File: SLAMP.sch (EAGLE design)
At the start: 45 parts, among them IC1 MEGA8-AI, J1 CARA1, J2 CARA4, J3 CARA2, J4 CARA5, J5 CARA3, J6 EXTRA-D12, J7 A0, Q1 2N7002PW, U1 HC_05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

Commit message: Placa empezada
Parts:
- JP2: value (none) -> CTS/RTS-bt
- JP3: value (none) -> POWER
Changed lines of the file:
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@@
 <part name="SUPPLY5" library="SparkFun-Aesthetics" deviceset="3.3V" device=""/>
 <part name="GND8" library="SparkFun-Aesthetics" deviceset="GND" device=""/>
-<part name="JP2" library="pinhead" deviceset="PINHD-1X2" device=""/>
+<part name="JP2" library="pinhead" deviceset="PINHD-1X2" device="" value="CTS/RTS-bt"/>
 <part name="GND9" library="SparkFun-Aesthetics" deviceset="GND" device=""/>
 <part name="SUPPLY1" library="SparkFun-Aesthetics" deviceset="5V" device=""/>
@@
 <part name="R5" library="SparkFun-Passives" deviceset="RESISTOR" device="0805-RES" value="1k"/>
 <part name="SUPPLY4" library="SparkFun-Aesthetics" deviceset="3.3V" device=""/>
-<part name="JP3" library="pinhead" deviceset="PINHD-1X2" device=""/>
+<part name="JP3" library="pinhead" deviceset="PINHD-1X2" device="" value="POWER"/>
 <part name="GND10" library="SparkFun-Aesthetics" deviceset="GND" device=""/>
 <part name="SUPPLY6" library="SparkFun-Aesthetics" deviceset="5V" device=""/>

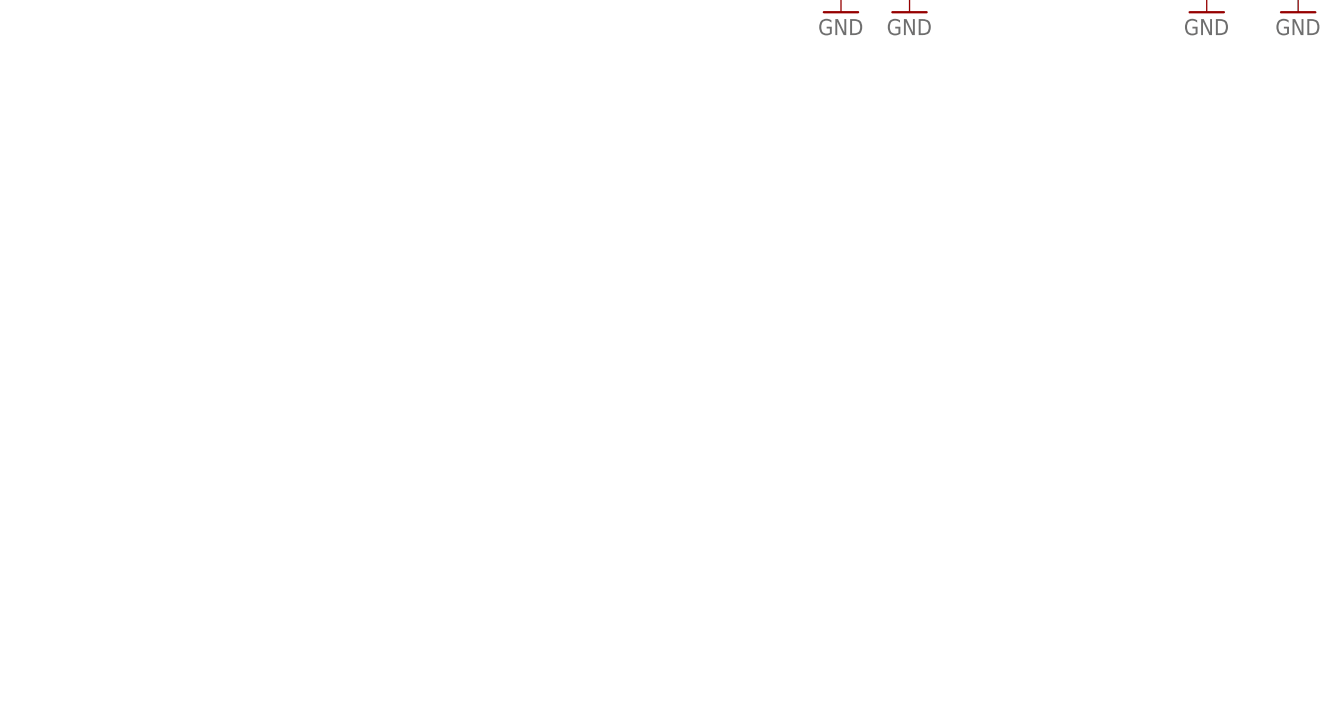
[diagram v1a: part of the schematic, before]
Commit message: capacitive touch sensor added
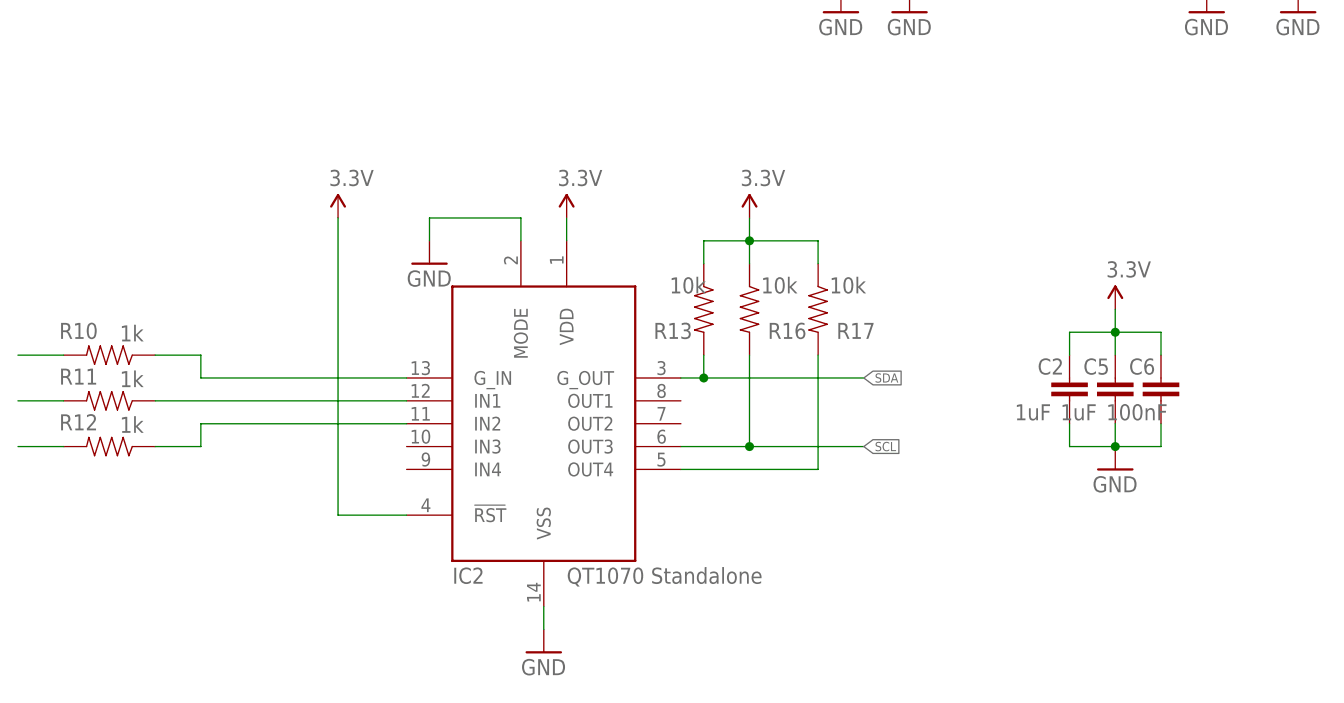
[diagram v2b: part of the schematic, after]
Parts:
- added C2, C5: 1uF, SparkFun-Passives:CAP0603-CAP
- added C6: 100nF, SparkFun-Passives:CAP0603-CAP
- added IC2: AT42QT1070-SSU, adafruit:AT42QT1070-SSU
- added R10, R11, R12: 1k, SparkFun-Passives:RESISTOR0603-RES
- added R13, R16, R17: 10k, SparkFun-Passives:RESISTOR0603-RES
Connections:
- new net N$1: IC2.OUT4, R17.2
- new net N$11: IC2.IN2, R12.1
- new net N$19: R10.2
- new net N$20: R11.2
- new net N$21: R12.2
- new net N$8: IC2.G_IN, R10.1
- new net N$9: IC2.IN1, R11.1
- new net SCL: IC2.OUT3, R16.2
- new net SDA: IC2.G_OUT, R13.2
- net 3.3V: now also C2.1, C5.1, C6.1, IC2.!RST, IC2.VDD, R13.1, R16.1, R17.1
- net GND: now also C2.2, C5.2, C6.2, IC2.MODE, IC2.VSS

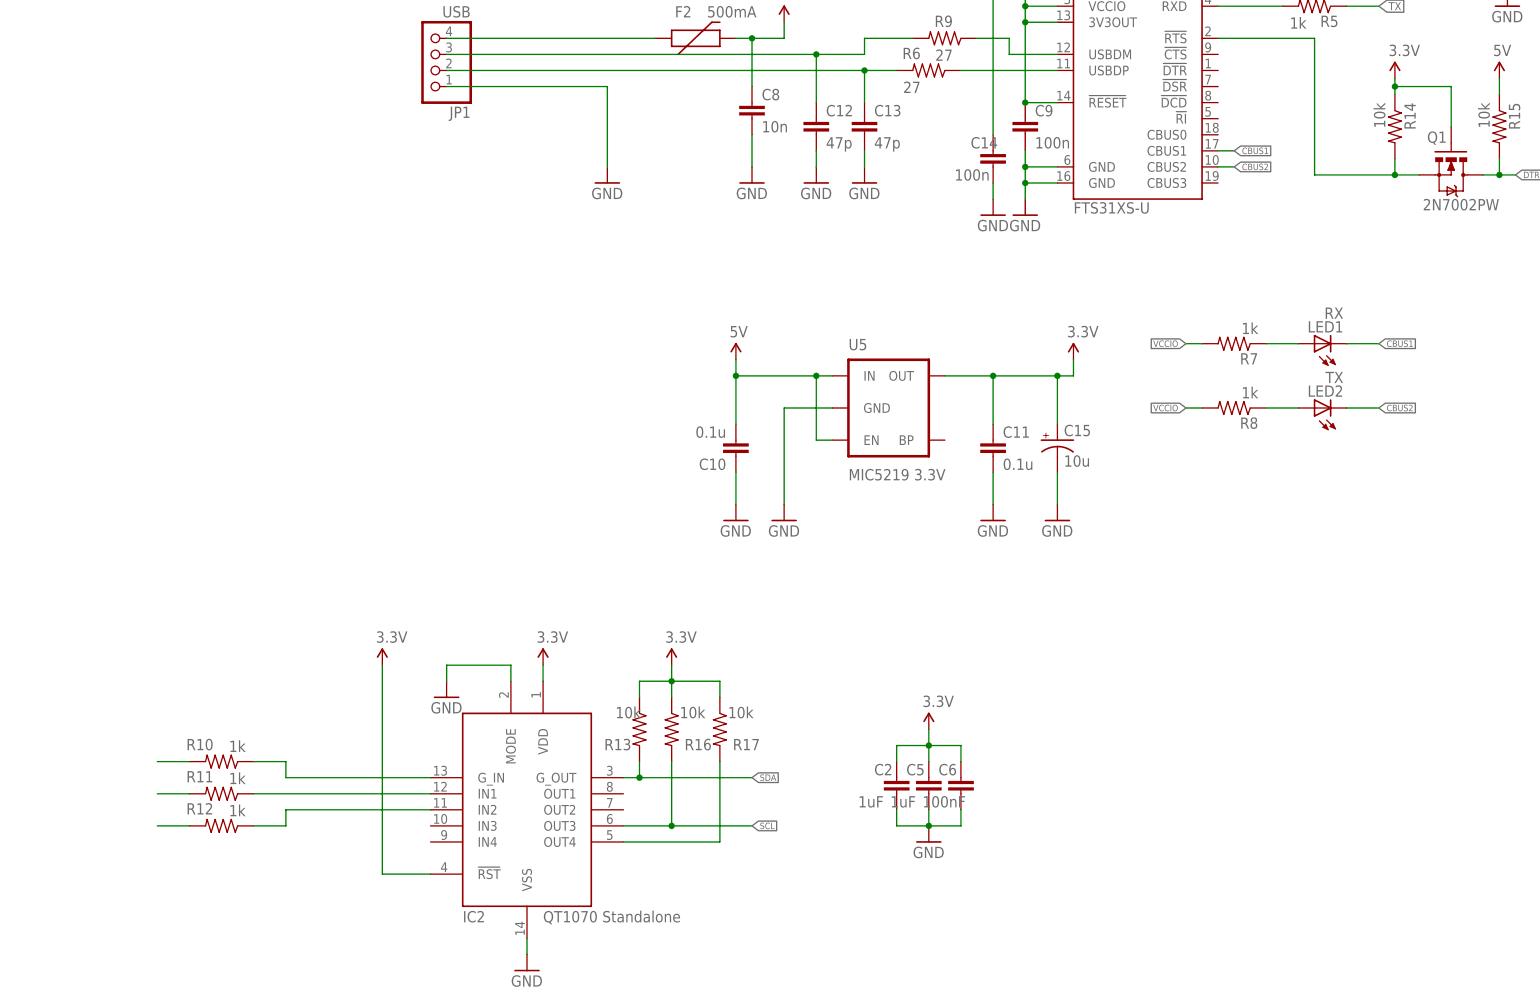
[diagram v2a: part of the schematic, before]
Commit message: LM358 added
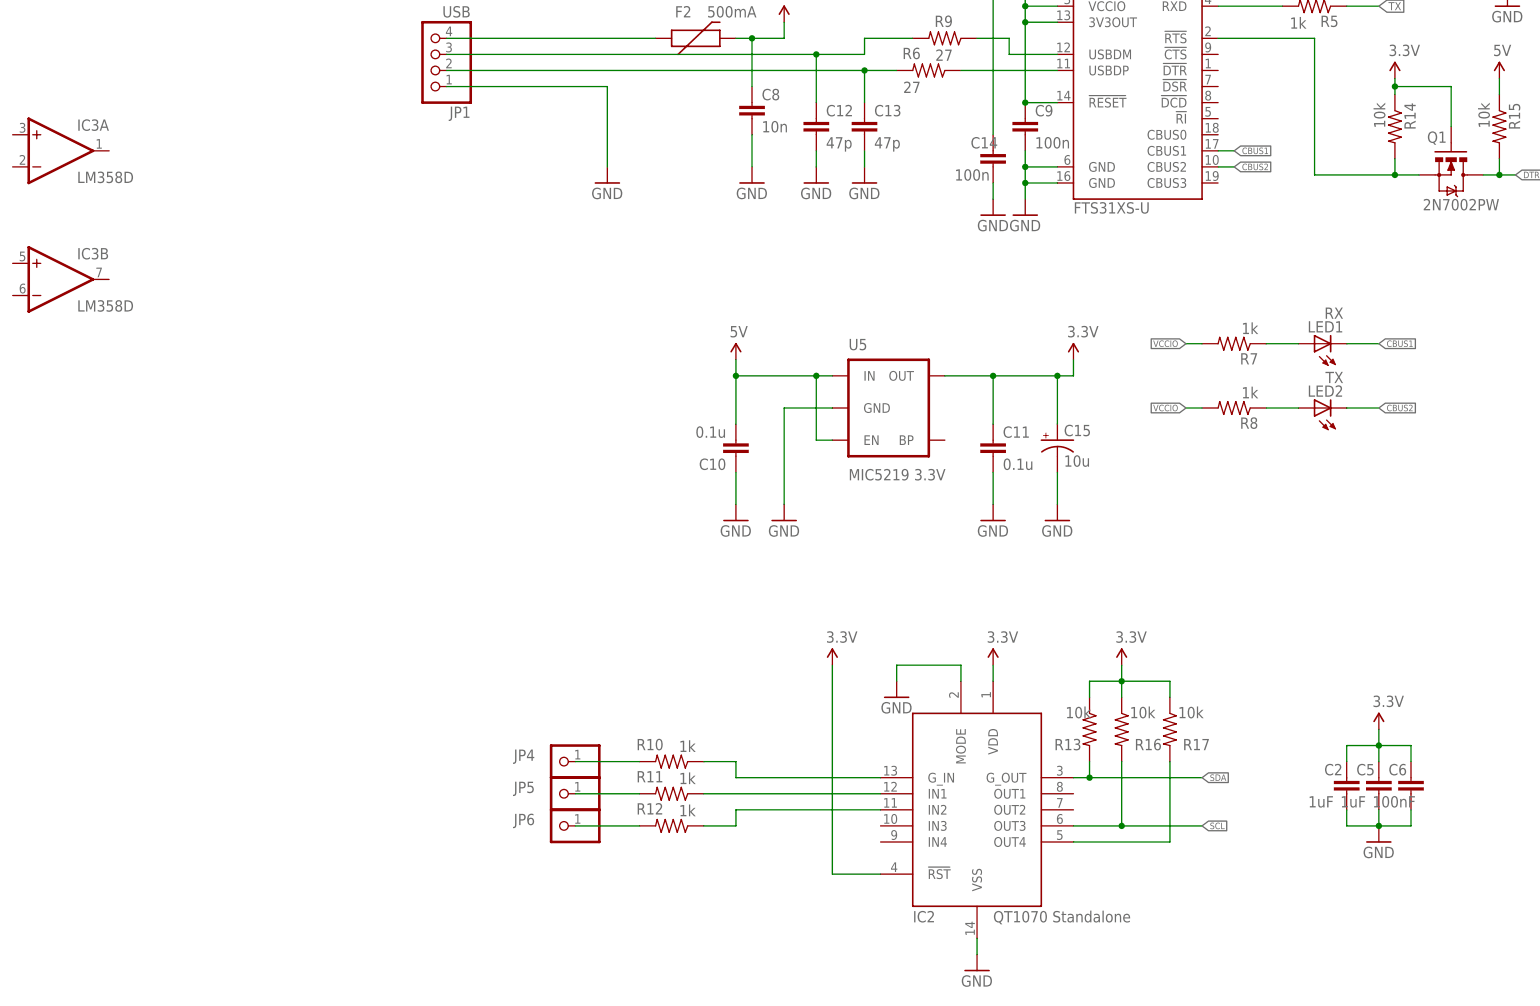
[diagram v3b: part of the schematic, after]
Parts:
- added IC3: LM358D, linear:LM358D
- added JP4, JP5, JP6: (no value), adafruit:PINHD-1X1
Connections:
- net N$19: now also JP4.1
- net N$20: now also JP5.1
- net N$21: now also JP6.1
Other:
- note added: "AT42QT1070-SSU operating in COMMS mode"
- note added: "To the "screws buttons" wires"
- moved on the sheet: C2, C5, C6, IC2, R10, R11, R12, R13, R16, R17

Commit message: Making some changes
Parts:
- removed IC3: LM358D, linear:LM358D
- removed JP6: (no value), adafruit:PINHD-1X1
- removed R1: 2k, SparkFun-Passives:RESISTOR0805-RES
- removed U5: MIC5219 3.3V, SparkFun-PowerIC:V_REG_MIC52193.3V
- added R26: 10k, SparkFun-Passives:RESISTOR0603-RES
- added U3: MIC5219 3.3V, SparkFun-PowerIC:V_REG_MIC52193.3V
- C1, C3: value 0.1u -> 100n
- C10, C11: value 0.1u -> 1uF
- C15: value 10u -> 100nF; device rcl:CPOL-USSMCP -> SparkFun-Passives:CAP0603-CAP
- C2, C5: value 1uF -> 0.1u
- C6: value 100nF -> 10u; device SparkFun-Passives:CAP0603-CAP -> rcl:CPOL-USSMCP
- JP2: value CTS/RTS-bt -> (none); device pinhead:PINHD-1X2 -> adafruit:PINHD-1X1
- LED1: value RX -> TX
- LED2: value TX -> RX
- R13: value 10k -> 1k
- R3: value 330 -> 1k
- R7: value 1k -> 2k; device SparkFun-Passives:RESISTOR0603-RES -> SparkFun-Passives:RESISTOR0805-RES
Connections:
- net B1 renamed B_TX
- net B2 renamed B_RX
- removed net CTS: JP2.1, U1.CTS
- removed net RTS: JP2.2, U1.RTS
- removed net STATE: R1.1, U1.PIO8
- new net BT_RX: IC1.PD3(INT1)
- new net BT_TX: IC1.PD2(INT0)
- new net D7: IC1.PD7(AIN1)
- new net D8: IC1.PB0(ICP)
- new net N$22: IC1.ADC7
- new net N$30: IC2.OUT4, R26.2
- new net N$7: IC1.ADC6
- net 3.3V: now also C10.1, C15.1, C6.+, R26.1, U3.OUT; no longer C15.+, C2.1, C6.1, R13.1, U5.OUT
- net 5V: now also C2.2, U3.EN, U3.IN; no longer C10.2, U5.EN, U5.IN
- net CBUS1: now also LED2.C; no longer LED1.C
- net CBUS2: now also LED1.C; no longer LED2.C
- net D12: no longer IC1.PB4(MISO)
- net D2: no longer IC1.PD2(INT0)
- net D3: no longer IC1.PD3(INT1)
- net GND: now also C10.2, C15.2, C2.1, C6.-, U3.GND; no longer C10.1, C15.-, C2.2, C6.2, U1.GND1, U5.GND
- net KEY: no longer U1.PIO11
- net N$1: now also R7.1, U1.PIO1; no longer IC2.OUT4, R17.2
- net N$10: now also LED2.A, R10.1; no longer D1.A, R1.2
- net N$11: now also IC2.G_IN, R11.1; no longer IC2.IN2, R12.1
- net N$12: now also IC2.IN1, R12.1; no longer LED2.A, R8.1
- net N$13: now also IC2.IN2, R13.1; no longer LED1.A, R7.1
- net N$19: now also JP2.1, R11.2; no longer JP4.1, R10.2
- net N$20: now also JP4.1, R12.2; no longer JP5.1, R11.2
- net N$21: now also JP5.1, R13.2; no longer JP6.1, R12.2
- net N$8: now also D1.A, R7.2; no longer IC2.G_IN, R10.1
- net N$9: now also LED1.A, R8.1; no longer IC2.IN1, R11.1
- net SCL: now also R17.2; no longer R16.2
- net SDA: now also R16.2; no longer R13.2
- net VCCIO: now also R10.2; no longer R7.2
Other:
- note added: "Bluetooth Connectivity"
- note added: "USB BRIDGE"
- moved on the sheet: C1, C10, C11, C12, C13, C14, C2, C3, C4, C5, C8, C9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
